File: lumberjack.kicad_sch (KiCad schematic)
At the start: 159 parts, among them J1 USB, J2 AVR_ISP_6, J3 JST, J4 JST, SW1 RESET, SW2 BOOT, U1 ATMEGA328-PU, Y1 16MHz

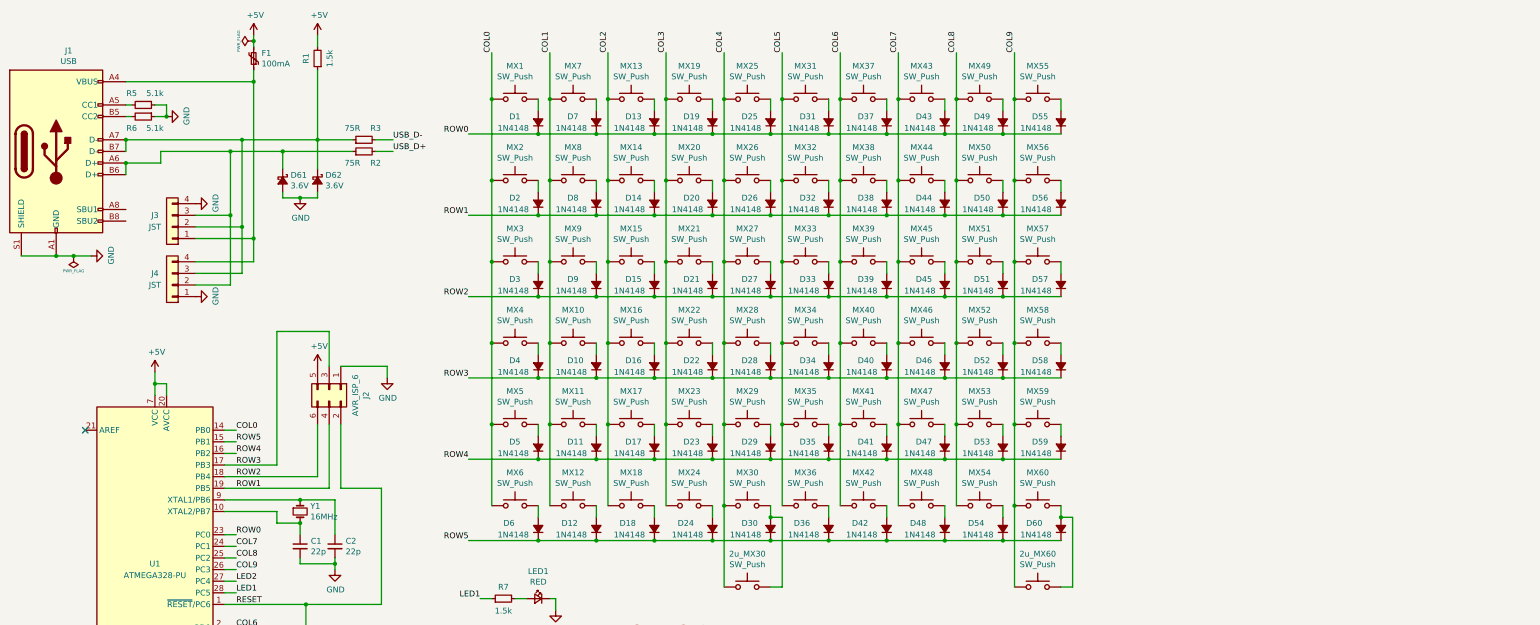
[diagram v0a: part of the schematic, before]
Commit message: add rows 13-17 to schematic
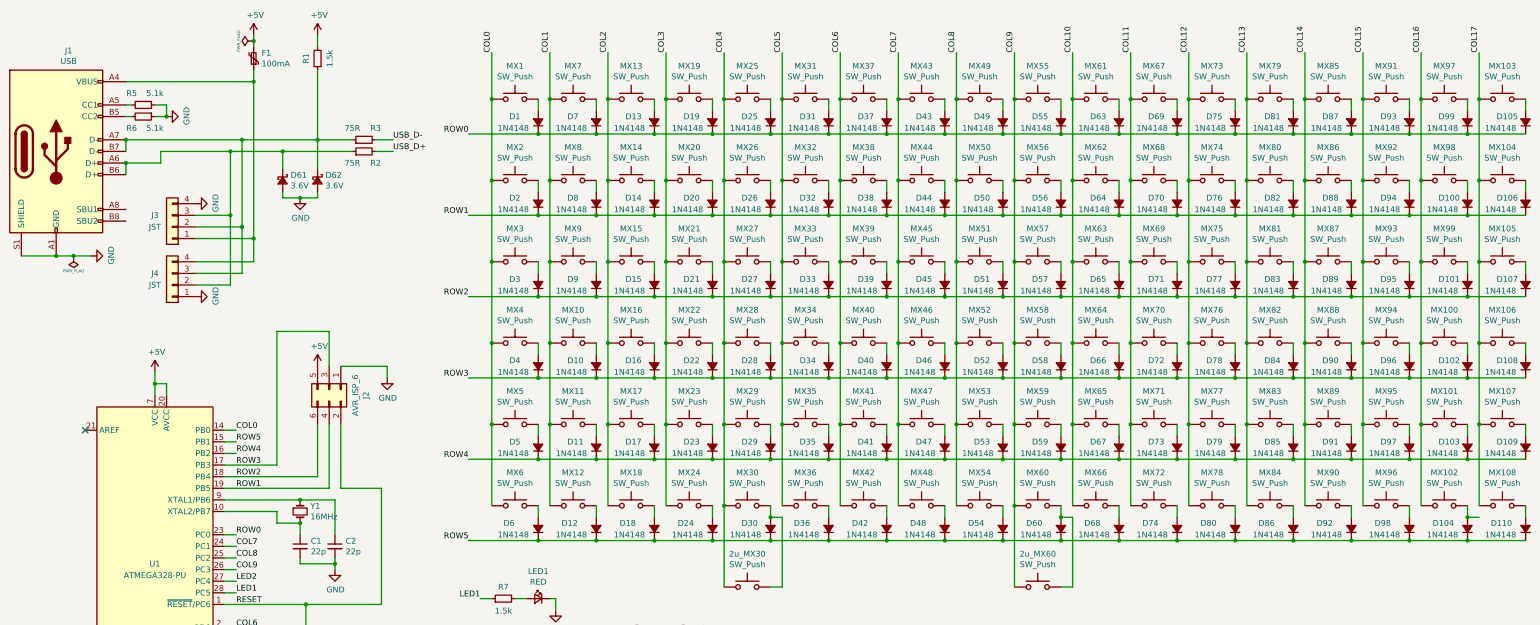
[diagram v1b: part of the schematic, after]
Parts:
- added D100, D101, D102, D103, D104, D105, D106, D107, D108, D109, D110, D63, D64, D65, D66, D67, D68, D69, D70, D71, D72, D73, D74, D75, D76, D77, D78, D79, D80, D81, D82, D83, D84, D85, D86, D87, D88, D89, D90, D91, D92, D93, D94, D95, D96, D97, D98, D99: 1N4148, Diode_THT:D_DO-35_SOD27_P7.62mm_Horizontal, symbol lumberjack-rescue:D_Small_ALT-Device
- added MX100, MX101, MX102, MX103, MX104, MX105, MX106, MX107, MX108, MX61, MX62, MX63, MX64, MX65, MX66, MX67, MX68, MX69, MX70, MX71, MX72, MX73, MX74, MX75, MX76, MX77, MX78, MX79, MX80, MX81, MX82, MX83, MX84, MX85, MX86, MX87, MX88, MX89, MX90, MX91, MX92, MX93, MX94, MX95, MX96, MX97, MX98, MX99: SW_Push, lumberjack:MX_Alps_Choc, symbol Switch:SW_Push
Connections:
- net ROW0: now also D105.1 (K), D63.1 (K), D69.1 (K), D75.1 (K), D81.1 (K), D87.1 (K), D93.1 (K), D99.1 (K)
- net ROW1: now also D100.1 (K), D106.1 (K), D64.1 (K), D70.1 (K), D76.1 (K), D82.1 (K), D88.1 (K), D94.1 (K)
- net ROW2: now also D101.1 (K), D107.1 (K), D65.1 (K), D71.1 (K), D77.1 (K), D83.1 (K), D89.1 (K), D95.1 (K)
- net ROW3: now also D102.1 (K), D108.1 (K), D66.1 (K), D72.1 (K), D78.1 (K), D84.1 (K), D90.1 (K), D96.1 (K)
- net ROW4: now also D103.1 (K), D109.1 (K), D67.1 (K), D73.1 (K), D79.1 (K), D85.1 (K), D91.1 (K), D97.1 (K)
- net ROW5: now also D104.1 (K), D110.1 (K), D68.1 (K), D74.1 (K), D80.1 (K), D86.1 (K), D92.1 (K), D98.1 (K)
- new net: D94.2 (A), MX92.1
- new net: D110.2 (A), MX108.1
- new net: D72.2 (A), MX70.1
- new net: D109.2 (A), MX107.1
- new net: D82.2 (A), MX80.1
- new net: D76.2 (A), MX74.1
- new net: D103.2 (A), MX101.1
- new net: D97.2 (A), MX95.1
- new net: D71.2 (A), MX69.1
- new net: D92.2 (A), MX90.1
- new net: D83.2 (A), MX81.1
- new net: D95.2 (A), MX93.1
- new net: D66.2 (A), MX64.1
- new net: D79.2 (A), MX77.1
- new net: D80.2 (A), MX78.1
- new net: D68.2 (A), MX66.1
- new net: D105.2 (A), MX103.1
- new net: D73.2 (A), MX71.1
- new net: D75.2 (A), MX73.1
- new net: D99.2 (A), MX97.1
- new net: D91.2 (A), MX89.1
- new net: D108.2 (A), MX106.1
- new net: D107.2 (A), MX105.1
- new net: D98.2 (A), MX96.1
- new net: D69.2 (A), MX67.1
- new net: D74.2 (A), MX72.1
- new net: D65.2 (A), MX63.1
- new net: D89.2 (A), MX87.1
- new net: D63.2 (A), MX61.1
- new net: D86.2 (A), MX84.1
- new net: D100.2 (A), MX98.1
- new net: D87.2 (A), MX85.1
- new net: D106.2 (A), MX104.1
- new net: D96.2 (A), MX94.1
- new net: D64.2 (A), MX62.1
- new net: D84.2 (A), MX82.1
- new net: D90.2 (A), MX88.1
- new net: D77.2 (A), MX75.1
- new net: D101.2 (A), MX99.1
- new net: D102.2 (A), MX100.1
- new net: D88.2 (A), MX86.1
- new net: D93.2 (A), MX91.1
- new net: D85.2 (A), MX83.1
- new net: D67.2 (A), MX65.1
- new net: D104.2 (A), MX102.1
- new net: D81.2 (A), MX79.1
- new net: D70.2 (A), MX68.1
- new net: D78.2 (A), MX76.1
- new net COL10: MX61.2, MX62.2, MX63.2, MX64.2, MX65.2, MX66.2
- new net COL11: MX67.2, MX68.2, MX69.2, MX70.2, MX71.2, MX72.2
- new net COL12: MX73.2, MX74.2, MX75.2, MX76.2, MX77.2, MX78.2
- new net COL13: MX79.2, MX80.2, MX81.2, MX82.2, MX83.2, MX84.2
- new net COL14: MX85.2, MX86.2, MX87.2, MX88.2, MX89.2, MX90.2
- new net COL15: MX91.2, MX92.2, MX93.2, MX94.2, MX95.2, MX96.2
- new net COL16: MX100.2, MX101.2, MX102.2, MX97.2, MX98.2, MX99.2
- new net COL17: MX103.2, MX104.2, MX105.2, MX106.2, MX107.2, MX108.2

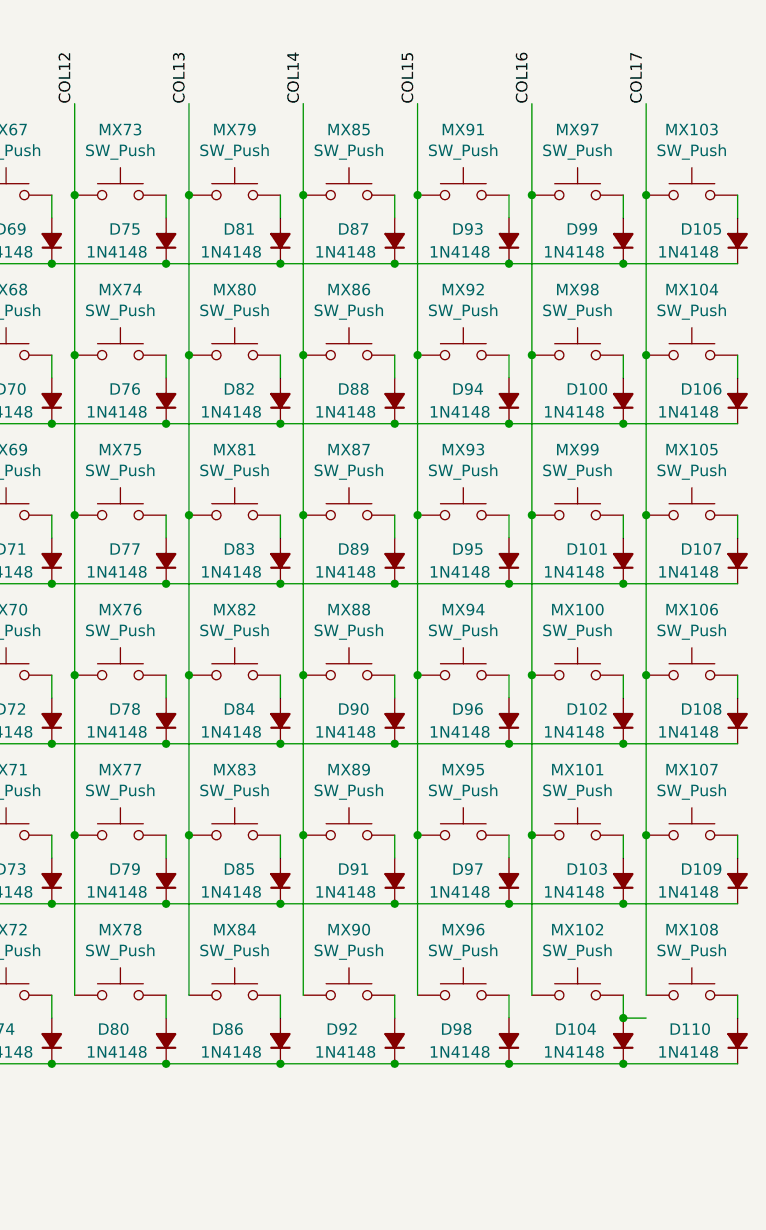
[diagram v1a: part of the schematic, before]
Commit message: truncate last col bc of uneven row layout
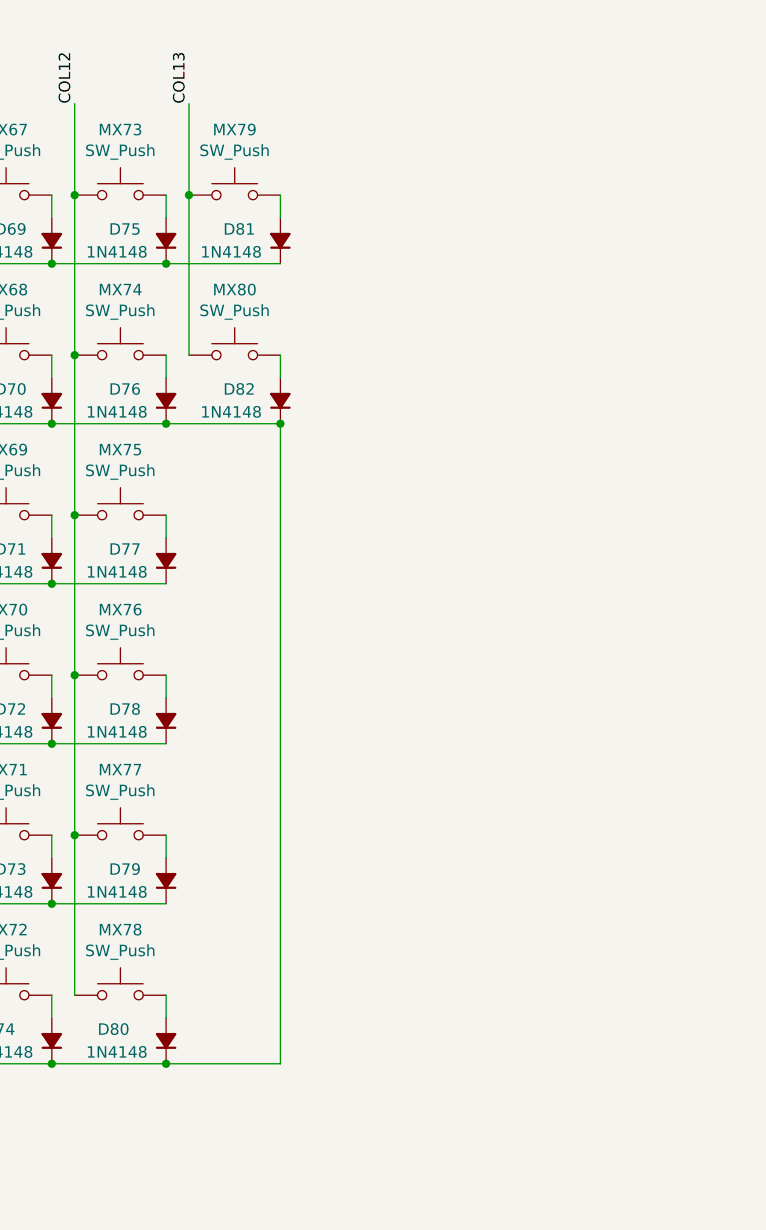
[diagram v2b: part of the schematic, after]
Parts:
- removed D100, D101, D102, D103, D104, D105, D106, D107, D108, D109, D110, D83, D84, D85, D86, D87, D88, D89, D90, D91, D92, D93, D94, D95, D96, D97, D98, D99: 1N4148, Diode_THT:D_DO-35_SOD27_P7.62mm_Horizontal, symbol lumberjack-rescue:D_Small_ALT-Device
- removed MX100, MX101, MX102, MX103, MX104, MX105, MX106, MX107, MX108, MX81, MX82, MX83, MX84, MX85, MX86, MX87, MX88, MX89, MX90, MX91, MX92, MX93, MX94, MX95, MX96, MX97, MX98, MX99: SW_Push, lumberjack:MX_Alps_Choc, symbol Switch:SW_Push
- MX1, MX10, MX11, MX12, MX13, MX14, MX15, MX16, MX17, MX18, MX19, MX2, MX20, MX21, MX22, MX23, MX24, MX25, MX26, MX27, MX28, MX29, MX3, MX30, MX31, MX32, MX33, MX34, MX35, MX36, MX37, MX38, MX39, MX4, MX40, MX41, MX42, MX43, MX44, MX45, MX46, MX47, MX48, MX49, MX5, MX50, MX51, MX52, MX53, MX54, MX55, MX56, MX57, MX58, MX59, MX6, MX60, MX61, MX62, MX63, MX64, MX65, MX66, MX67, MX68, MX69, MX7, MX70, MX71, MX72, MX73, MX74, MX75, MX76, MX77, MX78, MX79, MX80, MX9: footprint lumberjack:MX_Alps_Choc -> lumberjack:MX
- MX8: footprint lumberjack:MX_Alps_Choc_NTHSTH -> lumberjack:MX_NTHSTH
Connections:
- net ROW5 is gone; now on net ROW1: D12.1 (K), D18.1 (K), D24.1 (K), D30.1 (K), D36.1 (K), D42.1 (K), D48.1 (K), D54.1 (K), D6.1 (K), D60.1 (K), D68.1 (K), D74.1 (K), D80.1 (K), U1.15 (PB1)

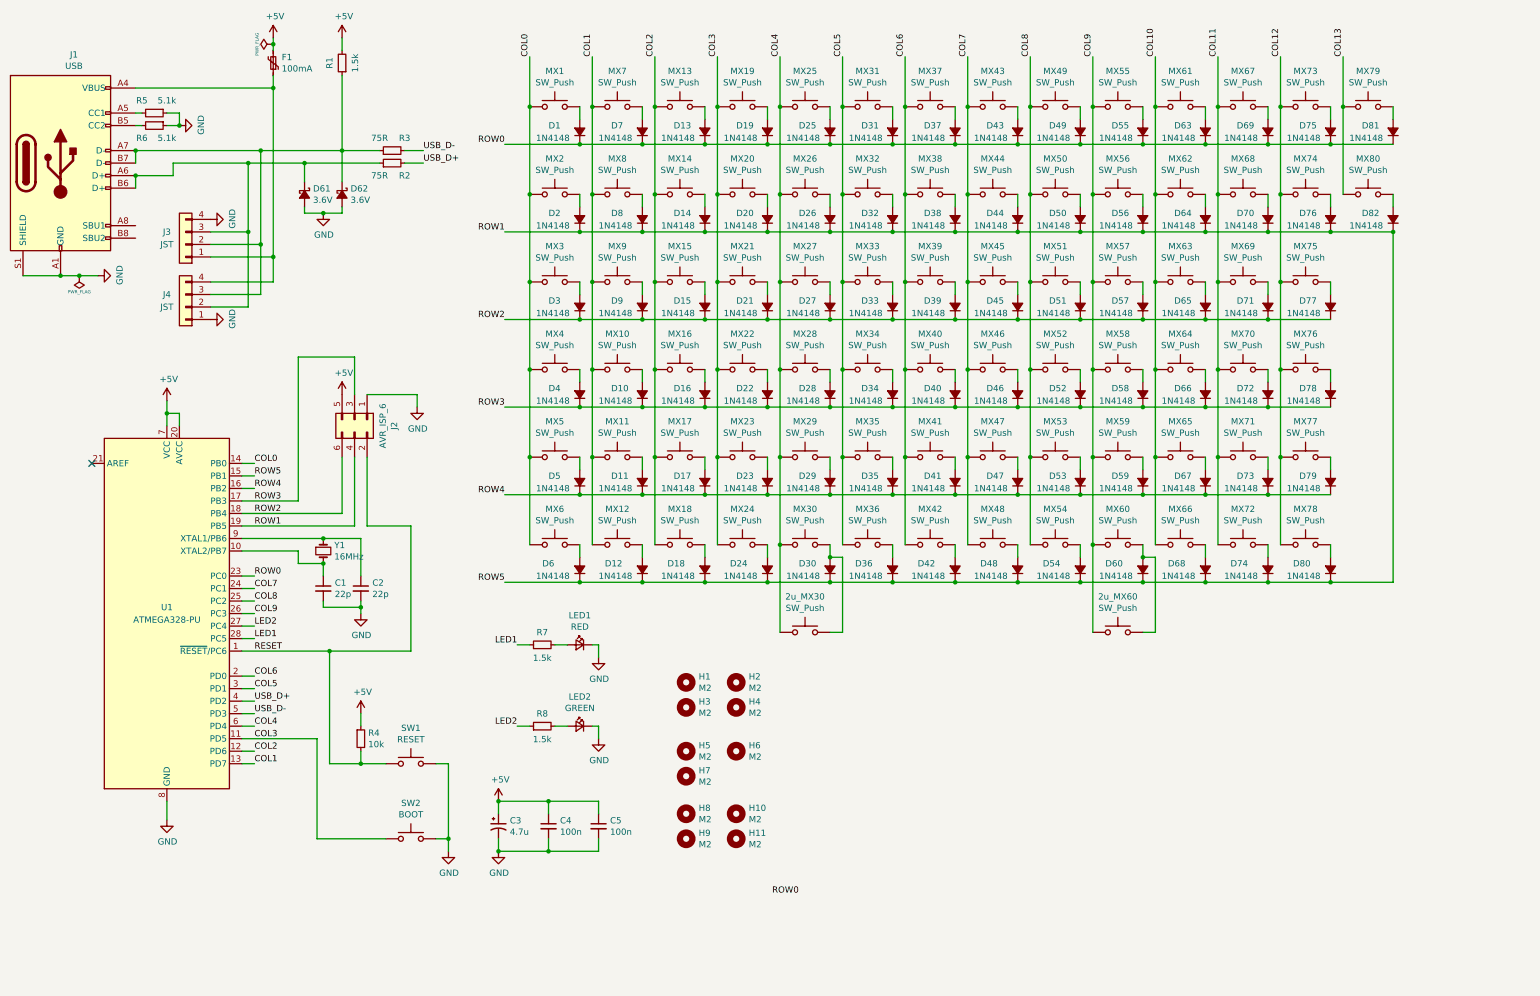
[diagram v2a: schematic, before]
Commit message: new IC and updated col layout
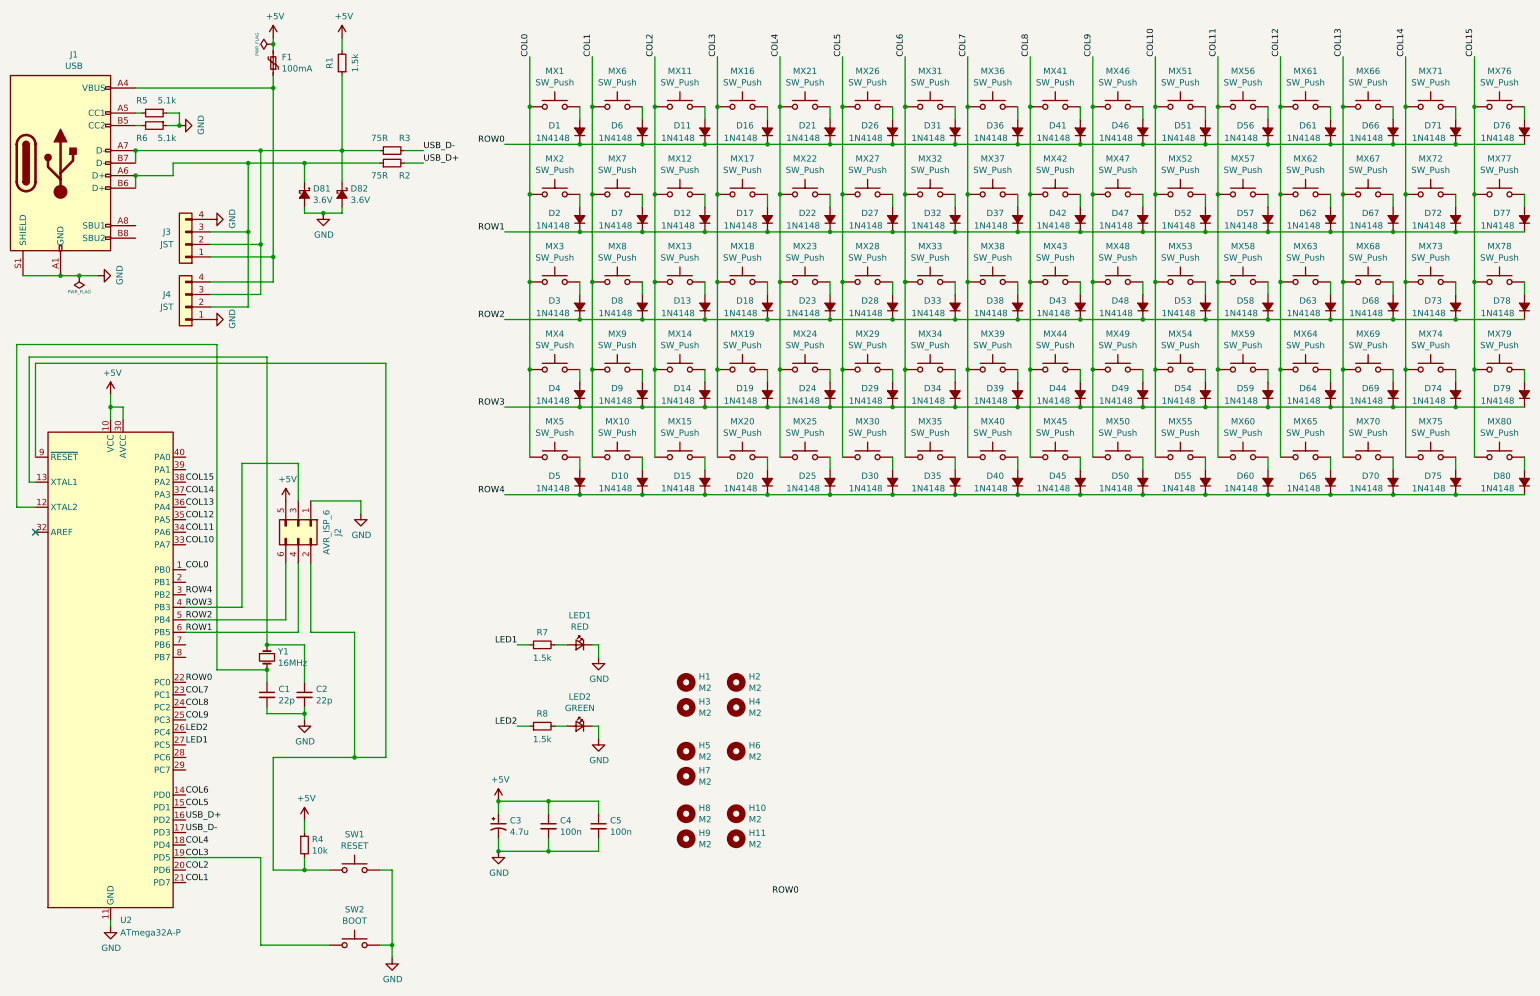
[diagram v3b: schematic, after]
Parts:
- removed 2u_MX30, 2u_MX60: SW_Push, lumberjack:MX_PCB_200B, symbol Switch:SW_Push
- removed D12, D18, D24, D30, D36, D42, D48, D54, D6, D60, D81, D82: 1N4148, Diode_THT:D_DO-35_SOD27_P7.62mm_Horizontal, symbol lumberjack-rescue:D_Small_ALT-Device
- removed MX12, MX18, MX24, MX30, MX36, MX42, MX48, MX54, MX6, MX60: SW_Push, lumberjack:MX, symbol Switch:SW_Push
- removed U1: ATMEGA328-PU, Package_DIP:DIP-28_W7.62mm, symbol lumberjack-rescue:ATmega328P-PU-MCU_Microchip_ATmega
- added D66, D67, D69, D70, D71, D72, D73, D75, D76, D77, D78, D79: 1N4148, Diode_THT:D_DO-35_SOD27_P7.62mm_Horizontal, symbol lumberjack-rescue:D_Small_ALT-Device
- added MX67, MX68, MX69, MX70, MX71, MX73, MX74, MX75, MX76, MX77: SW_Push, lumberjack:MX, symbol Switch:SW_Push
- added U2: ATmega32A-P, Package_DIP:DIP-40_W15.24mm, symbol MCU_Microchip_ATmega:ATmega32A-P
- renumbered D11 to D10, D13 to D11, D14 to D12, D15 to D13, D16 to D14, D17 to D15, D19 to D16, D20 to D17, D21 to D18, D22 to D19, D23 to D20, D25 to D21, D26 to D22, D27 to D23, D28 to D24, D29 to D25, D31 to D26, D32 to D27, D33 to D28, D34 to D29, D35 to D30, D37 to D31, D38 to D32, D39 to D33, D40 to D34, D41 to D35, D43 to D36, D44 to D37, D45 to D38, D46 to D39, D47 to D40, D49 to D41, D50 to D42, D51 to D43, D52 to D44, D53 to D45, D55 to D46, D56 to D47, D57 to D48, D58 to D49, D59 to D50, D63 to D51, D64 to D52, D65 to D53, D66 to D54, D67 to D55, D69 to D56, D70 to D57, D71 to D58, D72 to D59, D7 to D6, D73 to D60, D75 to D61, D76 to D62, D77 to D63, D78 to D64, D79 to D65, D8 to D7, D9 to D8, D61 to D81, D62 to D82, D10 to D9, MX11 to MX10, MX13 to MX11, MX14 to MX12, MX15 to MX13, MX16 to MX14, MX17 to MX15, MX19 to MX16, MX20 to MX17, MX21 to MX18, MX22 to MX19, MX23 to MX20, MX25 to MX21, MX26 to MX22, MX27 to MX23, MX28 to MX24, MX29 to MX25, MX31 to MX26, MX32 to MX27, MX33 to MX28, MX34 to MX29, MX35 to MX30, MX37 to MX31, MX38 to MX32, MX39 to MX33, MX40 to MX34, MX41 to MX35, MX43 to MX36, MX44 to MX37, MX45 to MX38, MX46 to MX39, MX47 to MX40, MX49 to MX41, MX50 to MX42, MX51 to MX43, MX52 to MX44, MX53 to MX45, MX55 to MX46, MX56 to MX47, MX57 to MX48, MX58 to MX49, MX59 to MX50, MX61 to MX51, MX62 to MX52, MX63 to MX53, MX64 to MX54, MX65 to MX55, MX67 to MX56, MX68 to MX57, MX69 to MX58, MX70 to MX59, MX7 to MX6, MX71 to MX60, MX73 to MX61, MX74 to MX62, MX75 to MX63, MX76 to MX64, MX77 to MX65, MX8 to MX7, MX9 to MX8, MX10 to MX9
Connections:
- net +5V: now also U2.10 (VCC), U2.30 (AVCC)
- net COL0: now also U2.1 (PB0)
- net COL1: now also U2.21 (PD7)
- net COL10: now also U2.33 (PA7); no longer MX66.2
- net COL11: now also U2.34 (PA6); no longer MX72.2
- net COL12: now also U2.35 (PA5); no longer MX78.2
- net COL13: now also MX66.2, MX67.2, MX68.2, MX69.2, MX70.2, U2.36 (PA4); no longer MX79.2, MX80.2
- net COL2: now also U2.20 (PD6)
- net COL3: now also U2.19 (PD5)
- net COL4: now also U2.18 (PD4)
- net COL5: now also U2.15 (PD1)
- net COL6: now also U2.14 (PD0)
- net COL7: now also U2.23 (PC1)
- net COL8: now also U2.24 (PC2)
- net COL9: now also U2.25 (PC3)
- net GND: now also U2.11 (GND), U2.31 (GND)
- net LED1: now also U2.27 (PC5)
- net LED2: now also U2.26 (PC4)
- net ROW0: now also D66.1 (K), D71.1 (K), D76.1 (K), U2.22 (PC0)
- net ROW1: now also D67.1 (K), D72.1 (K), D77.1 (K), U2.6 (PB5); no longer D68.1 (K), D74.1 (K), D80.1 (K)
- net ROW2: now also D68.1 (K), D73.1 (K), D78.1 (K), U2.5 (PB4)
- net ROW3: now also D74.1 (K), D69.1 (K), D79.1 (K), U2.4 (PB3)
- net ROW4: now also D80.1 (K), D70.1 (K), D75.1 (K), U2.3 (PB2)
- net USB_D+: now also U2.16 (PD2)
- net USB_D-: now also U2.17 (PD3)
- net at C1.1, Y1.2: now also U2.12 (XTAL2)
- net at C2.1, Y1.1: now also U2.13 (XTAL1)
- net at MX80.1: now also D80.2 (A)
- net at MX78.1: now also D78.2 (A); no longer D80.2 (A)
- net at MX66.1: now also D66.2 (A); no longer D68.2 (A)
- net at D74.2 (A): now also MX74.1; no longer MX72.1
- net at MX79.1: now also D79.2 (A)
- net RESET: no longer names the net of J2.2 (Pin_2), R4.2, SW1.1
- net RESET: now also U2.9 (~{RESET})
- new net: D72.2 (A), MX72.1
- new net: D76.2 (A), MX76.1
- new net: D67.2 (A), MX67.1
- new net: D73.2 (A), MX73.1
- new net: D77.2 (A), MX77.1
- new net: D69.2 (A), MX69.1
- new net: D71.2 (A), MX71.1
- new net: D68.2 (A), MX68.1
- new net: D70.2 (A), MX70.1
- new net: D75.2 (A), MX75.1
- new net COL14: MX71.2, MX72.2, MX73.2, MX74.2, MX75.2, U2.37 (PA3)
- new net COL15: MX76.2, MX77.2, MX78.2, MX79.2, MX80.2, U2.38 (PA2)

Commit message: new layout
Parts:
- removed D25, D40, D65, D70, D76, D77, D78, D79, D80: 1N4148, Diode_THT:D_DO-35_SOD27_P7.62mm_Horizontal, symbol lumberjack-rescue:D_Small_ALT-Device
- removed MX25, MX40, MX65, MX70, MX76, MX77, MX78, MX79, MX80: SW_Push, lumberjack:MX, symbol Switch:SW_Push
- added H12: M2, lumberjack:MountingHole_M2, symbol Mechanical:MountingHole
- MX10, MX15, MX20, MX45, MX5, MX50, MX55, MX60: footprint lumberjack:MX -> Button_Switch_Keyboard:SW_Cherry_MX_1.25u_PCB
- MX2, MX67: footprint lumberjack:MX -> Button_Switch_Keyboard:SW_Cherry_MX_1.50u_PCB
- MX3, MX30, MX35: footprint lumberjack:MX -> Button_Switch_Keyboard:SW_Cherry_MX_1.75u_PCB
- MX4, MX63: footprint lumberjack:MX -> Button_Switch_Keyboard:SW_Cherry_MX_2.25u_PCB
- MX59: footprint lumberjack:MX -> Button_Switch_Keyboard:SW_Cherry_MX_2.75u_PCB
- MX71: footprint lumberjack:MX -> Button_Switch_Keyboard:SW_Cherry_MX_2.00u_PCB
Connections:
- net ROW4 is gone; now on net ROW3: D10.1 (K), D15.1 (K), D20.1 (K), D30.1 (K), D35.1 (K), D45.1 (K), D5.1 (K), D50.1 (K), D55.1 (K), D60.1 (K), D75.1 (K), U2.3 (PB2)
